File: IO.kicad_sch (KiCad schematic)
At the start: 10 parts

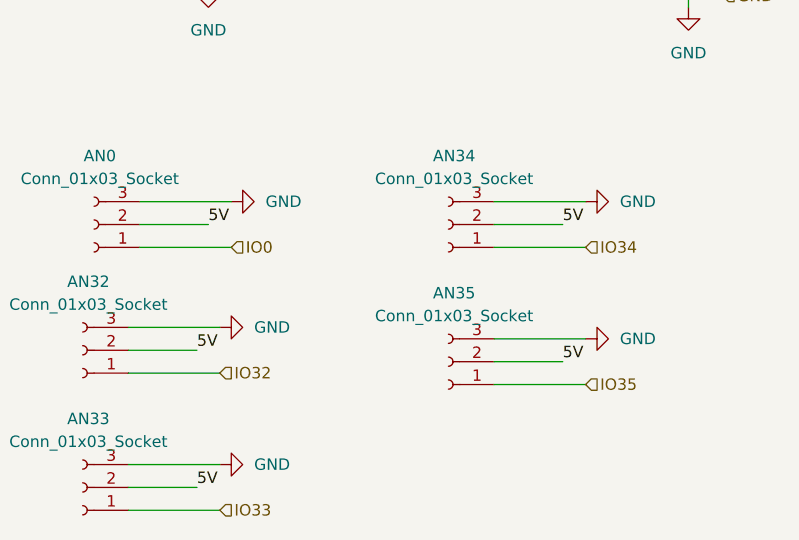
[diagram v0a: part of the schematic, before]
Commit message: en el esquematico coloque el brakeout del shifter, genere las librerias y simbolos, modifique los sensores que trabaja a 3.3 en el esquematico
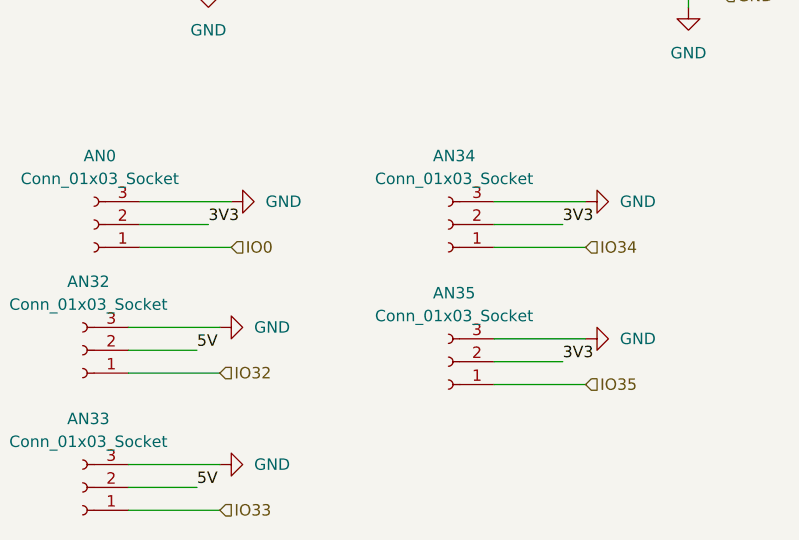
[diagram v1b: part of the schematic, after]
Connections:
- net 3V3: now also AN0.2 (Pin_2), AN34.2 (Pin_2), AN35.2 (Pin_2)
- net 5V: no longer AN0.2 (Pin_2), AN34.2 (Pin_2), AN35.2 (Pin_2)
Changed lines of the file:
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@@
 		)
 	)
-	(label "5V"
+	(label "3V3"
 		(at 185.42 118.11 0)
 		(effects
@@
 		)
 	)
-	(label "5V"
+	(label "3V3"
 		(at 185.42 102.87 0)
 		(effects
@@
 		)
 	)
-	(label "5V"
+	(label "3V3"
 		(at 146.05 102.87 0)
 		(effects

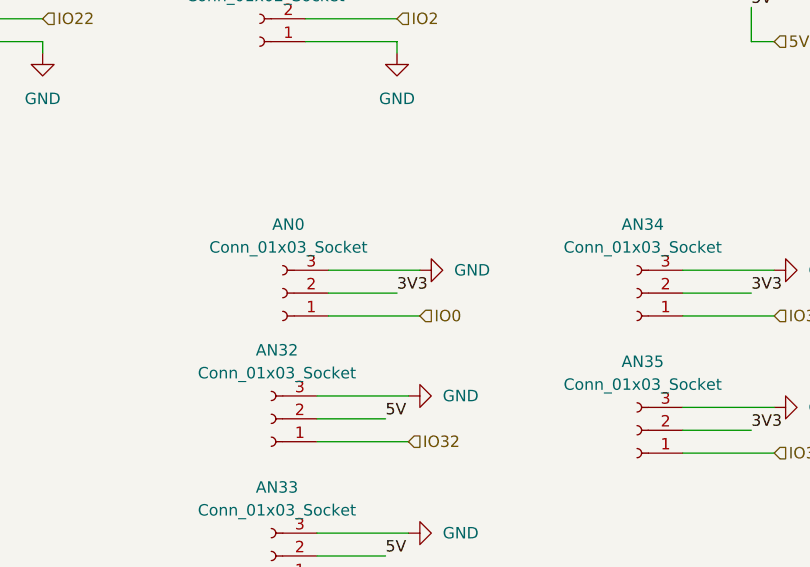
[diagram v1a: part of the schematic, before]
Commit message: feat: position of the components improved
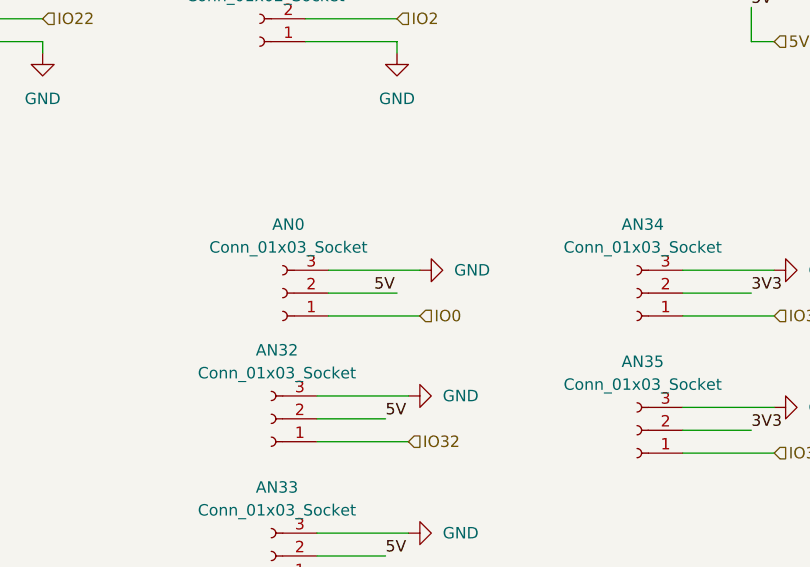
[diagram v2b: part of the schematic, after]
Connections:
- net 3V3: no longer AN0.2 (Pin_2)
- net 5V: now also AN0.2 (Pin_2)
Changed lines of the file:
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@@
+		)
+	)
+	(label "5V"
+		(at 143.51 102.87 0)
+		(effects
+			(font
+				(size 1.27 1.27)
+			)
+			(justify left bottom)
 		)
 	)
@@
 		(effects
 			(font
-				(size 1.27 1.27)
-			)
-			(justify left bottom)
-		)
-	)
-	(label "3V3"
-		(at 146.05 102.87 0)
-		(effects
-			(font
